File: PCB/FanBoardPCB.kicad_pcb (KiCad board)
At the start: 2 copper layers, 80 x 80 mm, 30 parts, among them J1 FAN2, J2 FAN1, J3 FAN4, J6 FanBrdConn, J7 FAN3, Q1 IRLML0030, Q2 IRLML0030, Q3 IRLML0030, Q4 IRLML0030

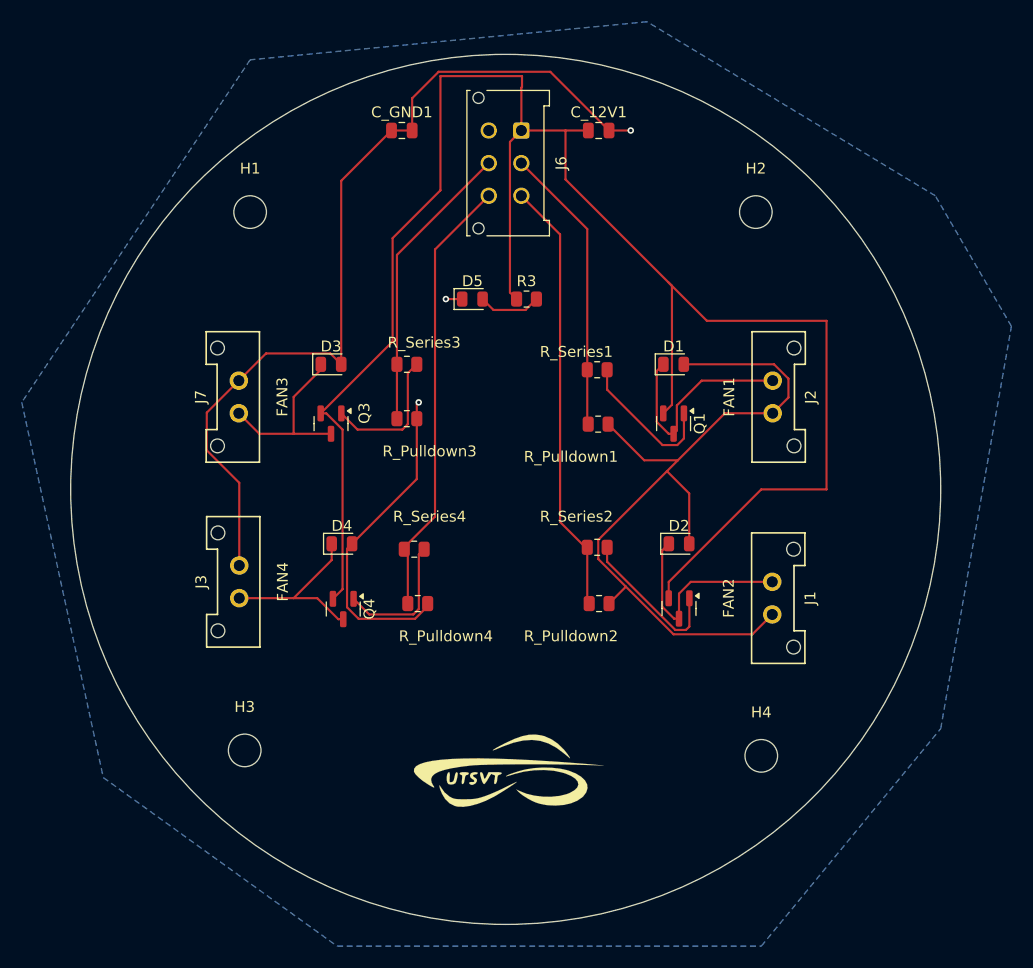
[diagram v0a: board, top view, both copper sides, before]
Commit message: updated traces
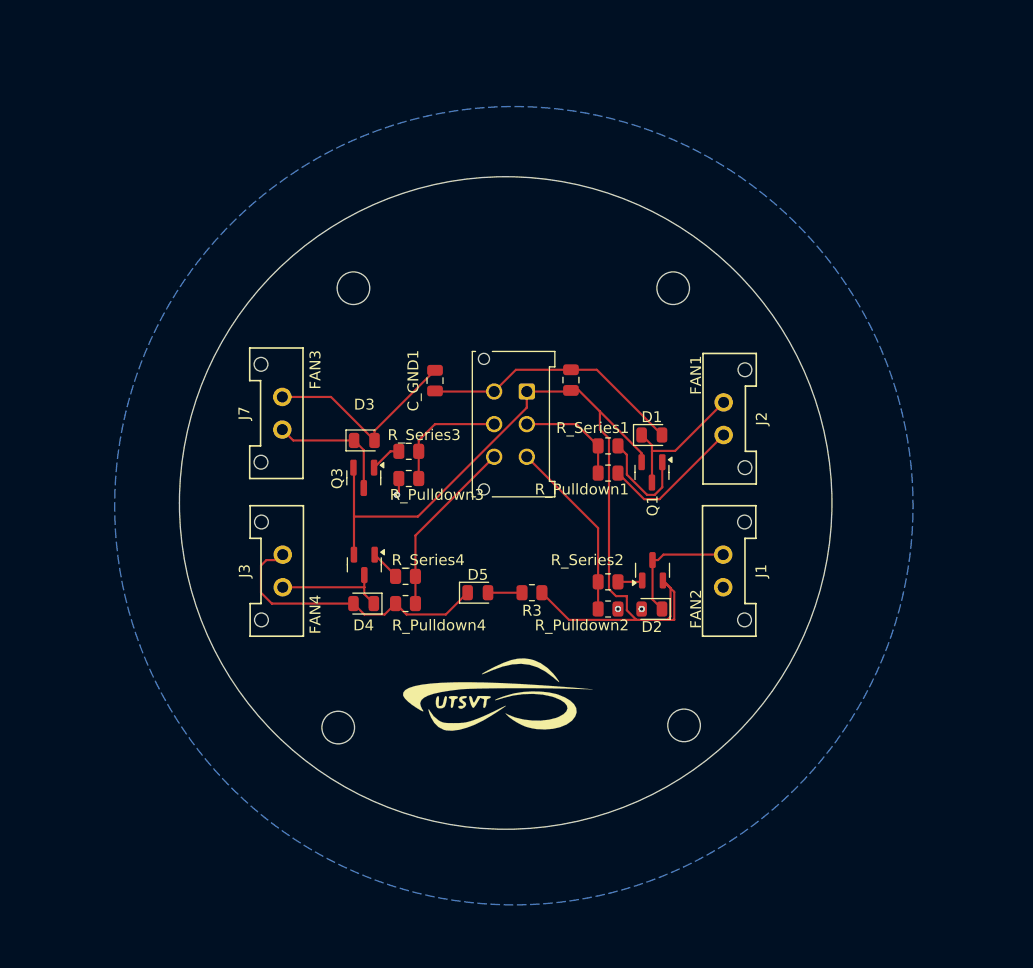
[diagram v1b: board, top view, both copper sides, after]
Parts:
- moved H2 47.7 mm to (169.4, 103.2)
- moved H4 43.8 mm to (168.4, 63.0)
- moved D5 27.0 mm to (150.4, 91.0)
- moved R3 27.0 mm to (155.4, 91.0), turned to 180 degrees
- moved J6 24.0 mm to (154.9, 72.5)
- moved C_GND1 23.2 mm to (146.5, 71.5), turned to 90 degrees
- moved C_12V1 23.1 mm to (159.0, 71.5), turned to 90 degrees
- moved H1 11.8 mm to (139.0, 63.0)
- moved H3 8.85 mm to (137.6, 103.4)
- moved R_Series3 8.00 mm to (144.1, 78.0), turned to 180 degrees
- moved D3 7.64 mm to (140.0, 77.0)
- moved G*** 7.07 mm to (152.0, 100.5)
- moved R_Series1 7.07 mm to (162.4, 77.5)
- moved D1 6.80 mm to (166.4, 76.5)
- moved D2 6.50 mm to (166.4, 92.5), turned to 180 degrees
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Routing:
- net GND: track 187.3 -> 84.2 mm
- net +12V: track 170.4 -> 88.6 mm
- net /FAN4: track 40.6 -> 16.5 mm
- net /FAN2: track 40.2 -> 16.7 mm
- net /FAN1: track 26.5 -> 10.0 mm
- net /FAN3: track 27.0 -> 11.1 mm
- net Net-(Q2-G): track 14.2 -> 2.28 mm
- net Net-(Q3-G): track 12.8 -> 2.90 mm
- net Net-(Q4-G): track 12.5 -> 2.80 mm
- net Net-(D2-K): track 19.4 -> 11.6 mm
- net Net-(D1-K): track 20.0 -> 13.2 mm
- net Net-(D4-K): track 16.8 -> 10.5 mm
- net Net-(D3-K): track 16.7 -> 11.8 mm
- net Net-(Q1-G): track 13.6 -> 9.60 mm
- net Net-(D5-A): track 5.78 -> 3.12 mm
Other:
- board size 80 x 80 mm -> 60 x 60 mm
- board text added: "FAN2"

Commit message: fixed trace width ??
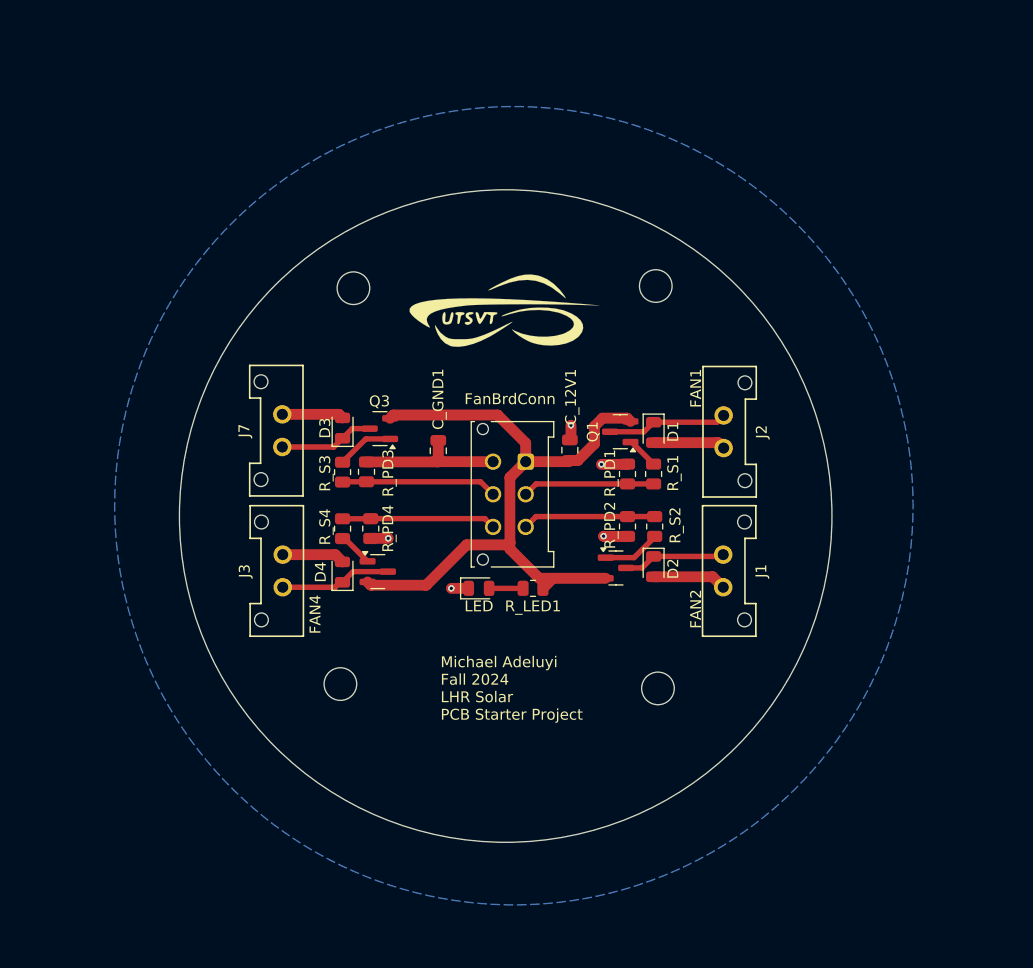
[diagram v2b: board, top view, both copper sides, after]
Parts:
- C_12V1, C_GND1: value C_Small -> 100u
- moved G*** 35.3 mm to (152.6, 65.2)
- moved R_PD2 7.80 mm to (164.2, 84.9), turned to -90 degrees
- moved R_PD4 7.60 mm to (140.6, 85.1), turned to -90 degrees
- moved R_S4 7.26 mm to (138.0, 85.1), turned to -90 degrees
- moved R_S2 6.65 mm to (166.7, 84.9), turned to -90 degrees
- moved C_GND1 6.46 mm to (146.8, 78.0)
- moved C_12V1 6.45 mm to (158.9, 77.9)
- moved J6 6.45 mm to (154.8, 79.0)
- moved R_S3 6.38 mm to (138.0, 79.9), turned to 90 degrees
- moved R_S1 4.92 mm to (166.6, 80.1), turned to 90 degrees
- moved Q3 4.76 mm to (141.4, 75.9), turned to 180 degrees
- moved Q1 4.74 mm to (163.5, 76.2), turned to 180 degrees
- moved H2 4.16 mm to (167.0, 99.8)
- moved H3 4.00 mm to (137.8, 99.4)
- moved R_PD3 3.94 mm to (140.2, 79.9), turned to 90 degrees
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- renumbered R3 to R_LED1, R_Pulldown1 to R_PD1, R_Pulldown2 to R_PD2, R_Pulldown3 to R_PD3, R_Pulldown4 to R_PD4, R_Series1 to R_S1, R_Series2 to R_S2, R_Series3 to R_S3, R_Series4 to R_S4
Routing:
- net GND: track 84.2 -> 47.7 mm, vias 3 -> 5
- net +12V: track 88.6 -> 62.4 mm
- net Net-(Q1-G): track 9.60 -> 3.14 mm
- net /FAN2: track 16.7 -> 12.3 mm
- net /FAN3: track 11.1 -> 14.3 mm
- net Net-(Q2-G): track 2.28 -> 5.34 mm
- net Net-(D3-K): track 11.8 -> 8.74 mm
- net Net-(Q3-G): track 2.90 -> 5.26 mm
- net /FAN4: track 16.5 -> 14.2 mm
- net Net-(D1-K): track 13.2 -> 11.1 mm
- net /FAN1: track 10.0 -> 12.2 mm
- net Net-(D2-K): track 11.6 -> 9.43 mm
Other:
- board text added: "C_12V1"
- board text added: "Michael Adeluyi Fall 2024 LHR Solar PCB Starter Project"
- board text added: "R_PD4"

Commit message: ye
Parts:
- moved H3 4.02 mm to (138.2, 103.4)
- moved H2 3.86 mm to (168.4, 103.4)
- moved H4 2.00 mm to (168.4, 64.0)
- moved H1 1.28 mm to (138.2, 64.0)
- moved G*** 0.41 mm to (153.0, 65.2)
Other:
- board text added: "FAN1"
- board text added: "FAN3"

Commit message: drc is happy
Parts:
- moved D2 0.20 mm to (166.6, 88.8)
- moved Q2 0.20 mm to (163.1, 88.9)
- moved R_PD2 0.20 mm to (164.2, 85.1)
- moved R_S2 0.20 mm to (166.7, 85.1)
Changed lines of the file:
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@@
 		(tags "diode")
 		(property "Reference" "D3"
-			(at 0 -1.6 90)
+			(at 2.4625 0 180)
 			(layer "F.SilkS")
 			(effects
@@
 		(tags "resistor")
 		(property "Reference" "R_PD1"
-			(at 0.0875 -1.6 90)
+			(at -1.9125 -3.4 180)
 			(layer "F.SilkS")
 			(effects
@@
 	(footprint "Diode_SMD:D_0805_2012Metric"
 		(layer "F.Cu")
-		(at 166.6 88.6 -90)
+		(at 166.6 88.8 -90)
 		(descr "Diode SMD 0805 (2012 Metric), square (rectangular) end terminal, IPC_7351 nominal, (Body size source: https://docs.google.com/spreadsheets/d/1BsfQQcO9C6DZCsRaXUlFlo91Tg2WpOkGARC1WS5S8t0/edit?usp=sharing), generated with kicad-footprint-generator")
 		(tags "diode")
 		(property "Reference" "D2"
-			(at 0.2 -1.8 90)
+			(at 2.4 -0.2 180)
 			(layer "F.SilkS")
 			(effects
@@
 	(footprint "Package_TO_SOT_SMD:SOT-23"
 		(layer "F.Cu")
-		(at 163.1375 88.725)
+		(at 163.1375 88.925)
 		(descr "SOT, 3 Pin (https://www.jedec.org/system/files/docs/to-236h.pdf variant AB), generated with kicad-footprint-generator ipc_gullwing_generator.py")
 		(tags "SOT TO_SOT_SMD")
@@
 	(footprint "Resistor_SMD:R_0805_2012Metric"
 		(layer "F.Cu")
-		(at 164.2 84.9125 -90)
+		(at 164.2 85.1125 -90)
 		(descr "Resistor SMD 0805 (2012 Metric), square (rectangular) end terminal, IPC_7351 nominal, (Body size source: IPC-SM-782 page 72, https://www.pcb-3d.com/wordpress/wp-content/uploads/ipc-sm-782a_amendment_1_and_2.pdf), generated with kicad-footprint-generator")
 		(tags "resistor")
 		(property "Reference" "R_PD2"
-			(at -0.1125 1.6 90)
+			(at -1.7125 3.4 180)
 			(layer "F.SilkS")
 			(effects
@@
 		)
 		(property "Value" "FAN4"
-			(at 1.7 -3.5 90)
+			(at 1.7 -3.3 90)
 			(layer "F.SilkS")
 			(effects
@@
 		(tags "resistor")
 		(property "Reference" "R_PD3"
-			(at -0.1125 2 90)
+			(at -1.9125 3.8 180)
 			(layer "F.SilkS")
 			(effects
@@
 	(footprint "Resistor_SMD:R_0805_2012Metric"
 		(layer "F.Cu")
-		(at 166.7 84.9125 -90)
+		(at 166.7 85.1125 -90)
 		(descr "Resistor SMD 0805 (2012 Metric), square (rectangular) end terminal, IPC_7351 nominal, (Body size source: IPC-SM-782 page 72, https://www.pcb-3d.com/wordpress/wp-content/uploads/ipc-sm-782a_amendment_1_and_2.pdf), generated with kicad-footprint-generator")
 		(tags "resistor")
@@
 		(tags "SOT TO_SOT_SMD")
 		(property "Reference" "Q1"
-			(at 2.5375 0 90)
+			(at -0.0625 2.6 180)
 			(layer "F.SilkS")
 			(effects
@@
 		)
 		(property "Value" "LED"
-			(at 0 1.65 0)
+			(at 0 1.8 0)
 			(layer "F.SilkS")
 			(effects
@@
 	)
 	(gr_text "FAN2"
-		(at 175.8 89 270)
+		(at 176 89 270)
 		(layer "F.SilkS")
 		(effects
@@
 	)
 	(gr_text "R_PD4"
-		(at 142.1925 85.105 90)
+		(at 144 83.2 0)
 		(layer "F.SilkS")
 		(effects
@@
 	)
 	(gr_text "FAN3"
-		(at 129.4 76.2 90)
+		(at 129.2 76.1 90)
 		(layer "F.SilkS")
 		(effects
@@
 	)
 	(segment
-		(start 158.8 78.95)
-		(end 158.9 78.85)
+		(start 156.465 89.875)
+		(end 155.895 89.305)
 		(width 1)
 		(layer "F.Cu")
@@
 	)
 	(segment
-		(start 153.39 86.4)
-		(end 153.39 86.99)
-		(width 1)
-		(layer "F.Cu")
-		(net 1)
-	)
-	(segment
-		(start 162.2 89.675)
-		(end 157.35 89.675)
+		(start 158.8 78.95)
+		(end 158.9 78.85)
 		(width 1)
 		(layer "F.Cu")
@@
 	)
 	(segment
+		(start 156.425 89.835)
+		(end 156.425 90.6)
+		(width 1)
+		(layer "F.Cu")
+		(net 1)
+	)
+	(segment
+		(start 162.2 89.875)
+		(end 156.465 89.875)
+		(width 1)
+		(layer "F.Cu")
+		(net 1)
+	)
+	(segment
 		(start 154.84 78.95)
 		(end 158.8 78.95)
@@
 	)
 	(segment
-		(start 157.35 89.675)
-		(end 156.425 90.6)
-		(width 1)
-		(layer "F.Cu")
-		(net 1)
-	)
-	(segment
 		(start 149.4 86.6)
 		(end 153.19 86.6)
@@
 	)
 	(segment
-		(start 156.075 89.675)
-		(end 157.35 89.675)
+		(start 154.84 78.95)
+		(end 153.39 80.4)
 		(width 1)
 		(layer "F.Cu")
@@
 	)
 	(segment
-		(start 154.84 78.95)
-		(end 153.39 80.4)
+		(start 153.19 86.6)
+		(end 155.895 89.305)
 		(width 1)
 		(layer "F.Cu")
@@
 	)
 	(segment
-		(start 161.1625 75.693762)
-		(end 161.906261 74.950001)
+		(start 155.895 89.305)
+		(end 156.425 89.835)
 		(width 1)
 		(layer "F.Cu")
@@
 	)
 	(segment
-		(start 153.39 86.99)
-		(end 156.075 89.675)
+		(start 161.1625 75.693762)
+		(end 161.906261 74.950001)
 		(width 1)
 		(layer "F.Cu")
@@
 	)
 	(segment
-		(start 166.6 89.5375)
-		(end 172.0375 89.5375)
-		(width 1)
-		(layer "F.Cu")
-		(net 2)
-	)
-	(segment
 		(start 159 76.85)
 		(end 158.9 76.95)
@@
 	)
 	(segment
-		(start 162.025 85.825)
-		(end 162 85.8)
+		(start 161.8 79.2)
+		(end 164.175 79.2)
 		(width 1)
 		(layer "F.Cu")
@@
 	)
 	(segment
-		(start 161.8 79.2)
-		(end 164.175 79.2)
+		(start 146.85 78.95)
+		(end 146.8 78.9)
 		(width 1)
 		(layer "F.Cu")
@@
 	)
 	(segment
-		(start 146.85 78.95)
-		(end 146.8 78.9)
+		(start 166.6 89.7375)
+		(end 172.2375 89.7375)
+		(width 1)
+		(layer "F.Cu")
+		(net 2)
+	)
+	(segment
+		(start 172.2375 89.7375)
+		(end 173 90.5)
 		(width 1)
 		(layer "F.Cu")
@@
 	)
 	(segment
+		(start 162 86)
+		(end 164.175 86)
+		(width 1)
+		(layer "F.Cu")
+		(net 2)
+	)
+	(segment
 		(start 140.61 86)
 		(end 140.5925 86.0175)
@@
 	)
 	(segment
-		(start 172.0375 89.5375)
-		(end 173 90.5)
-		(width 1)
-		(layer "F.Cu")
-		(net 2)
-	)
-	(segment
-		(start 164.2 85.825)
-		(end 162.025 85.825)
+		(start 164.175 86)
+		(end 164.2 86.025)
 		(width 1)
 		(layer "F.Cu")
@@
 	)
 	(via
-		(at 162 85.8)
+		(at 162 86)
 		(size 0.6)
 		(drill 0.3)
@@
 	)
 	(segment
-		(start 165.5375 88.725)
-		(end 166.6 87.6625)
+		(start 165.5375 88.925)
+		(end 166.6 87.8625)
 		(width 0.5)
 		(layer "F.Cu")
@@
 	)
 	(segment
-		(start 166.6 87.6625)
-		(end 172.8375 87.6625)
+		(start 172.6375 87.8625)
+		(end 166.6 87.8625)
 		(width 0.5)
 		(layer "F.Cu")
@@
 	)
 	(segment
-		(start 172.8375 87.6625)
-		(end 173 87.5)
+		(start 173 87.5)
+		(end 172.6375 87.8625)
 		(width 0.5)
 		(layer "F.Cu")
@@
 	)
 	(segment
-		(start 164.075 88.725)
-		(end 165.5375 88.725)
+		(start 164.075 88.925)
+		(end 165.5375 88.925)
 		(width 0.5)
 		(layer "F.Cu")
@@
 	)
 	(segment
-		(start 164.2 84)
-		(end 166.7 84)
+		(start 164.2 84.2)
+		(end 166.7 84.2)
 		(width 0.5)
 		(layer "F.Cu")
@@
 	)
 	(segment
-		(start 155.79 84)
+		(start 155.59 84.2)
 		(end 154.84 84.95)
 		(width 0.5)
@@
 	)
 	(segment
-		(start 164.2 84)
-		(end 155.79 84)
+		(start 164.2 84.2)
+		(end 155.59 84.2)
 		(width 0.5)
 		(layer "F.Cu")
@@
 	)
 	(segment
-		(start 166.7 85.874636)
-		(end 166.7 85.825)
+		(start 166.7 86.074636)
+		(end 166.7 86.025)
 		(width 0.5)
 		(layer "F.Cu")
@@
 	)
 	(segment
-		(start 162.2 87.775)
-		(end 164.799636 87.775)
+		(start 164.799636 87.975)
+		(end 162.2 87.975)
 		(width 0.5)
 		(layer "F.Cu")
@@
 	)
 	(segment
-		(start 164.799636 87.775)
-		(end 166.7 85.874636)
+		(start 164.799636 87.975)
+		(end 166.7 86.074636)
 		(width 0.5)
 		(layer "F.Cu")

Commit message: added a guy on it
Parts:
- added G***: LOGO, my-images:pointing guy 10mm, F.Cu at (162.8, 99.2)

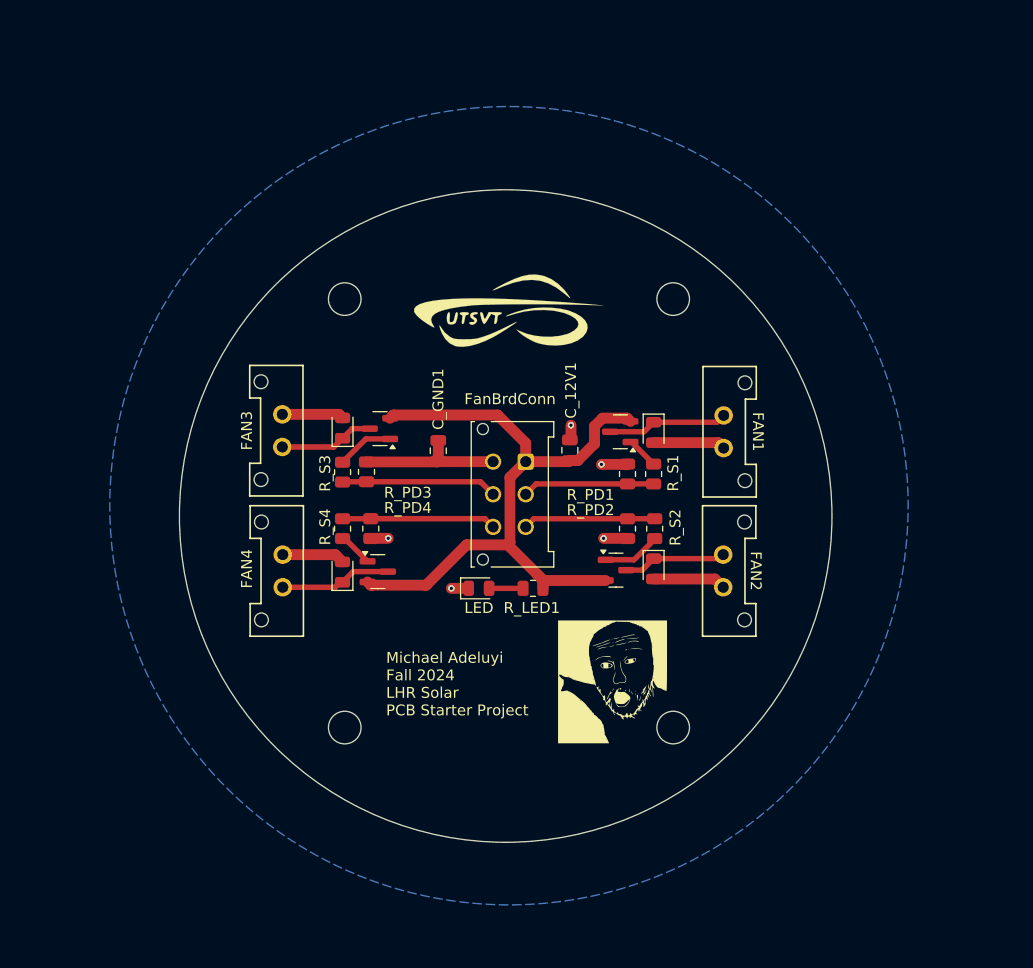
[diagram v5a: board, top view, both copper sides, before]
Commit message: added top 12V and bottom GND planes
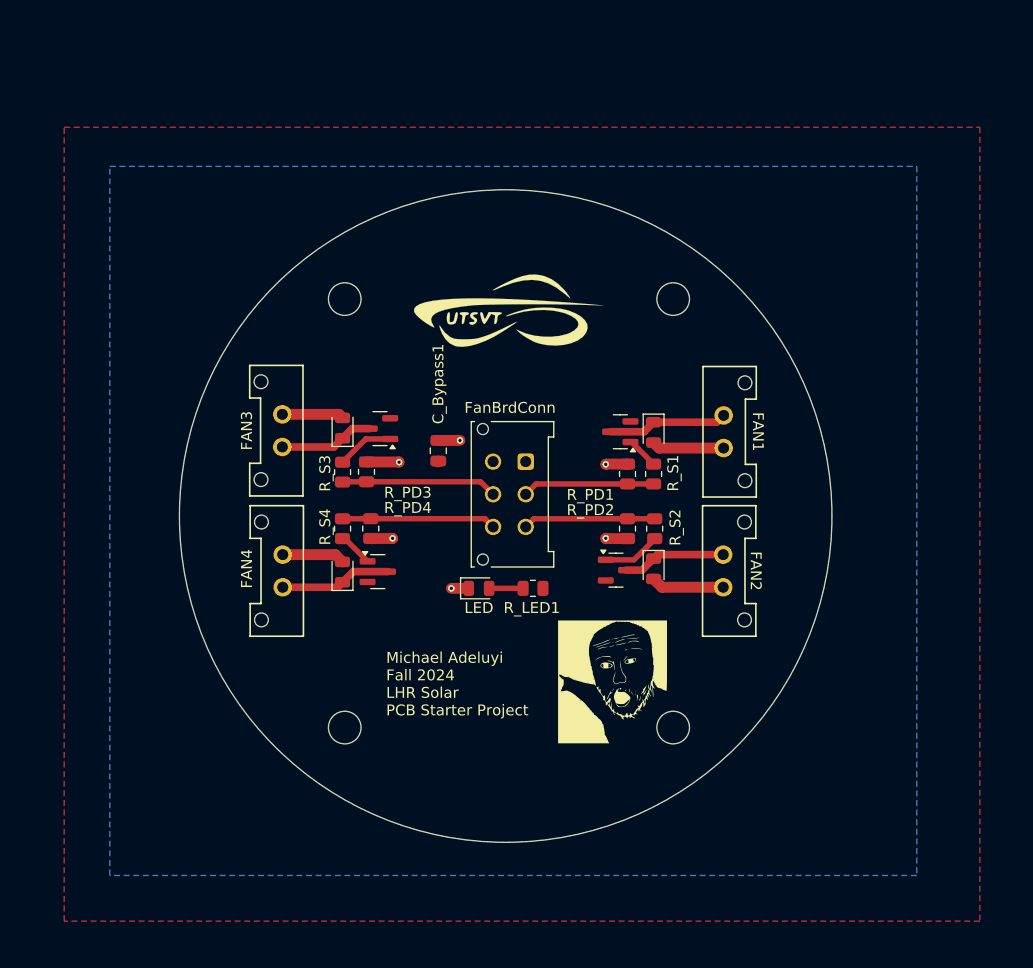
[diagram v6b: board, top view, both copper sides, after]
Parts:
- removed C_12V1: 100u, Capacitor_SMD:C_0805_2012Metric
- renumbered C_GND1 to C_Bypass1
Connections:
- C_Bypass1 pad 1: GND -> +12V
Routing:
- net +12V: track 62.5 -> 0.18 mm
- net GND: track 47.6 -> 37.5 mm, vias 5 -> 6
- added copper zone on F.Cu, net +12V
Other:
- board text removed: "C_12V1"
